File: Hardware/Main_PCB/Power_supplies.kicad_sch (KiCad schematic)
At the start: 21 parts, among them U2 TPS62170DSG, U3 TPS61175PWPR, U7 BD50FD0WFP2-E2

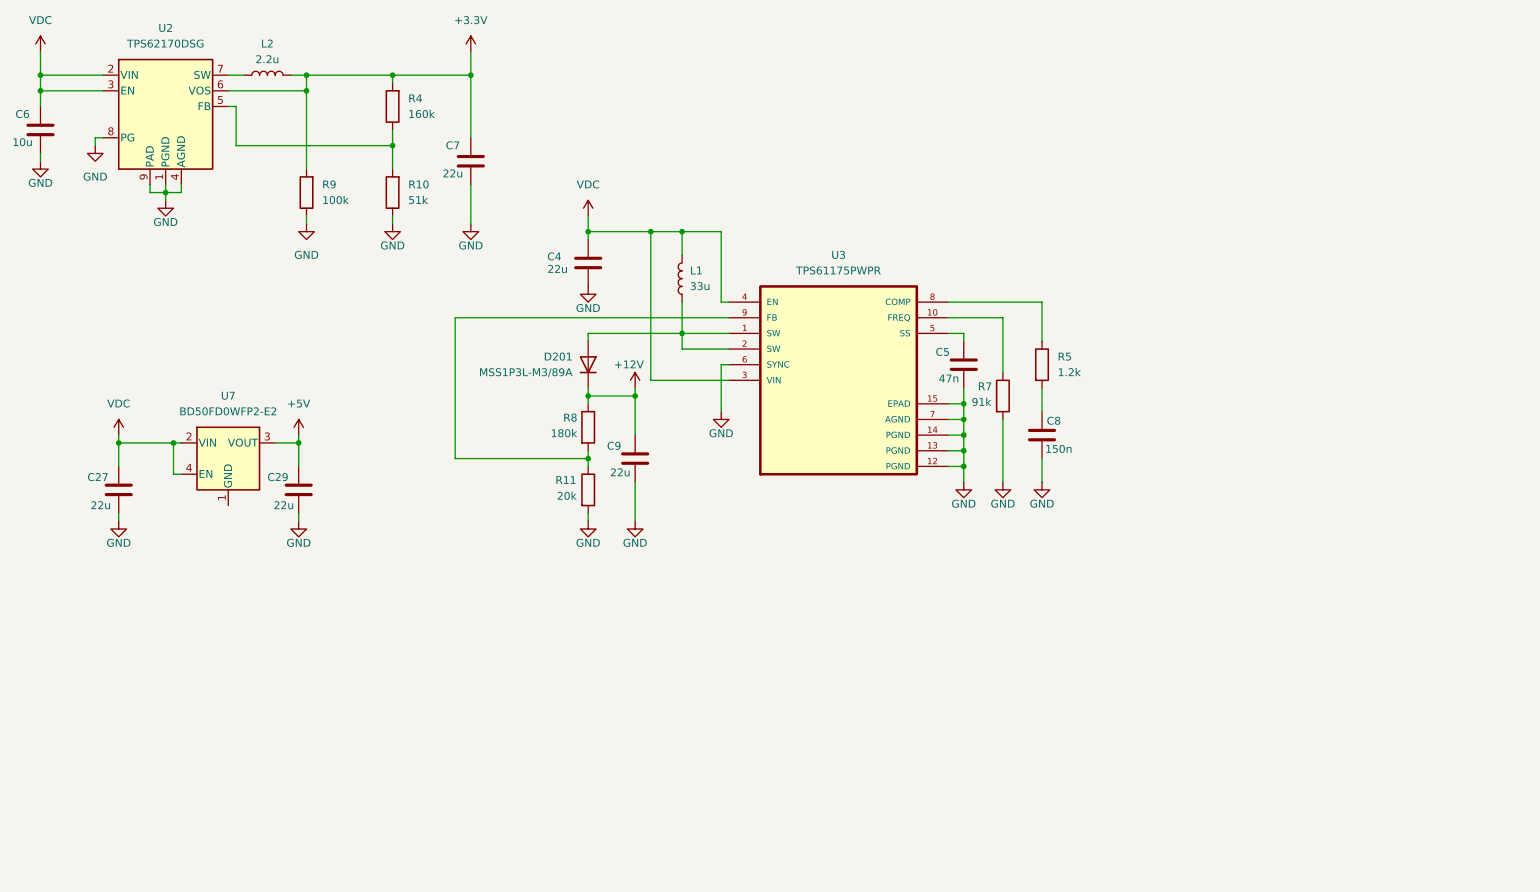
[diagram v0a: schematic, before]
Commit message: A finished version of the Main PCB schematic
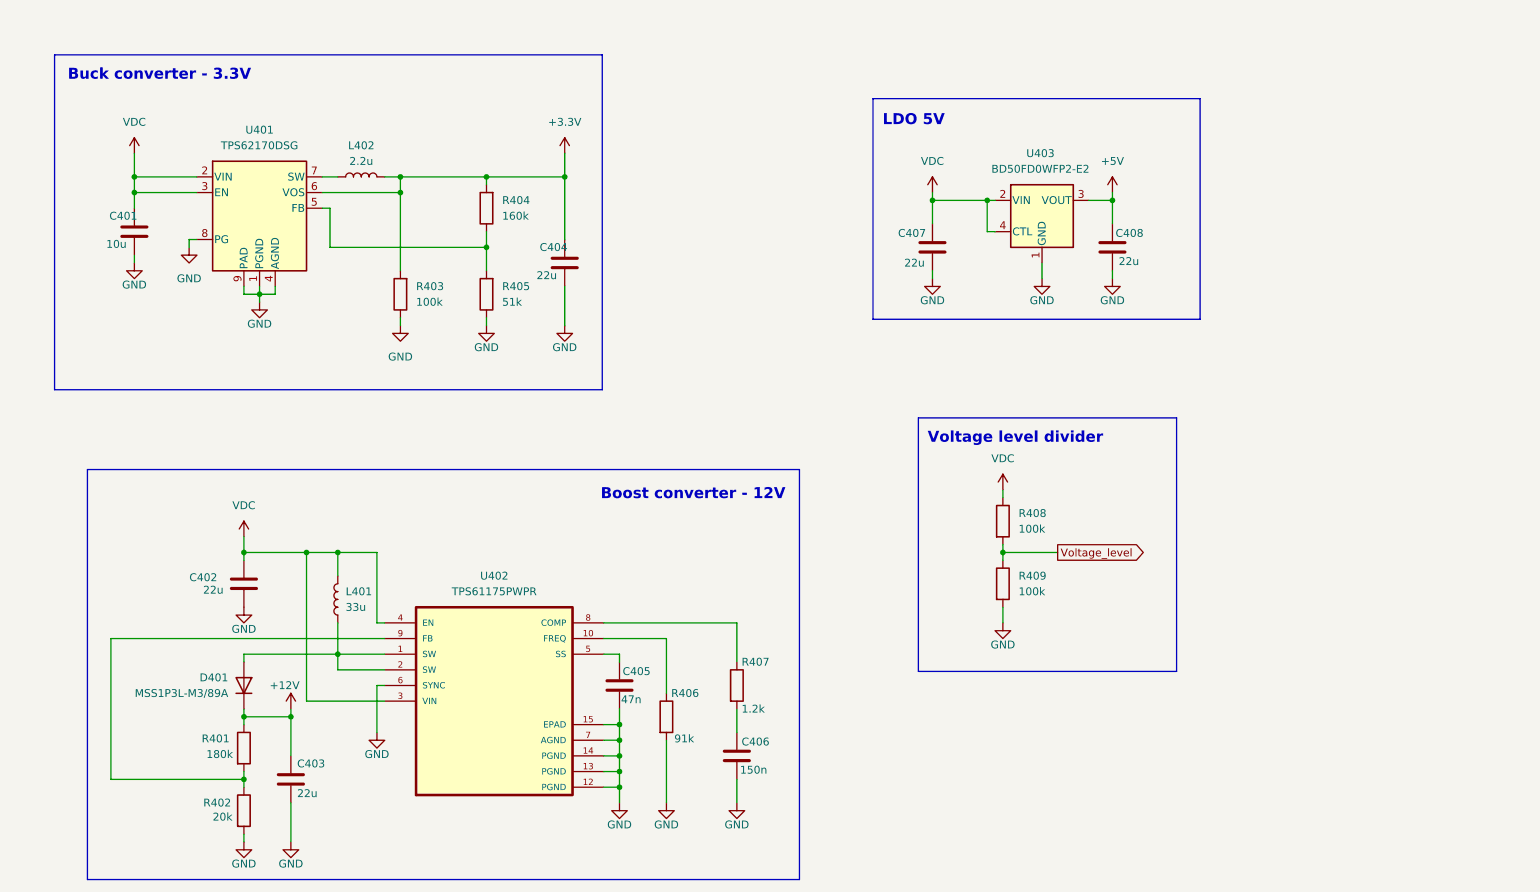
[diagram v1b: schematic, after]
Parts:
- added R408, R409: 100k, Resistor_SMD:R_0603_1608Metric_Pad0.98x0.95mm_HandSolder, symbol Device:R
- renumbered C6 to C401, C4 to C402, C9 to C403, C7 to C404, C5 to C405, C8 to C406, C27 to C407, C29 to C408, D201 to D401, L1 to L401, L2 to L402, R8 to R401, R11 to R402, R9 to R403, R4 to R404, R10 to R405, R7 to R406, R5 to R407, U2 to U401, U3 to U402, U7 to U403
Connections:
- net GND: now also U403.1 (GND), R409.2
- net VDC: now also R408.1
- new net Voltage_level: R408.2, R409.1
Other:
- note added: "Boost converter - 12V"
- note added: "Buck converter - 3.3V"
- note added: "LDO 5V"
- note added: "Voltage level divider"
- moved on the sheet: C401, C402, C403, C404, C405, C406, C407, C408, D401, L401, L402, R401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

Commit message: Added footprints to all components
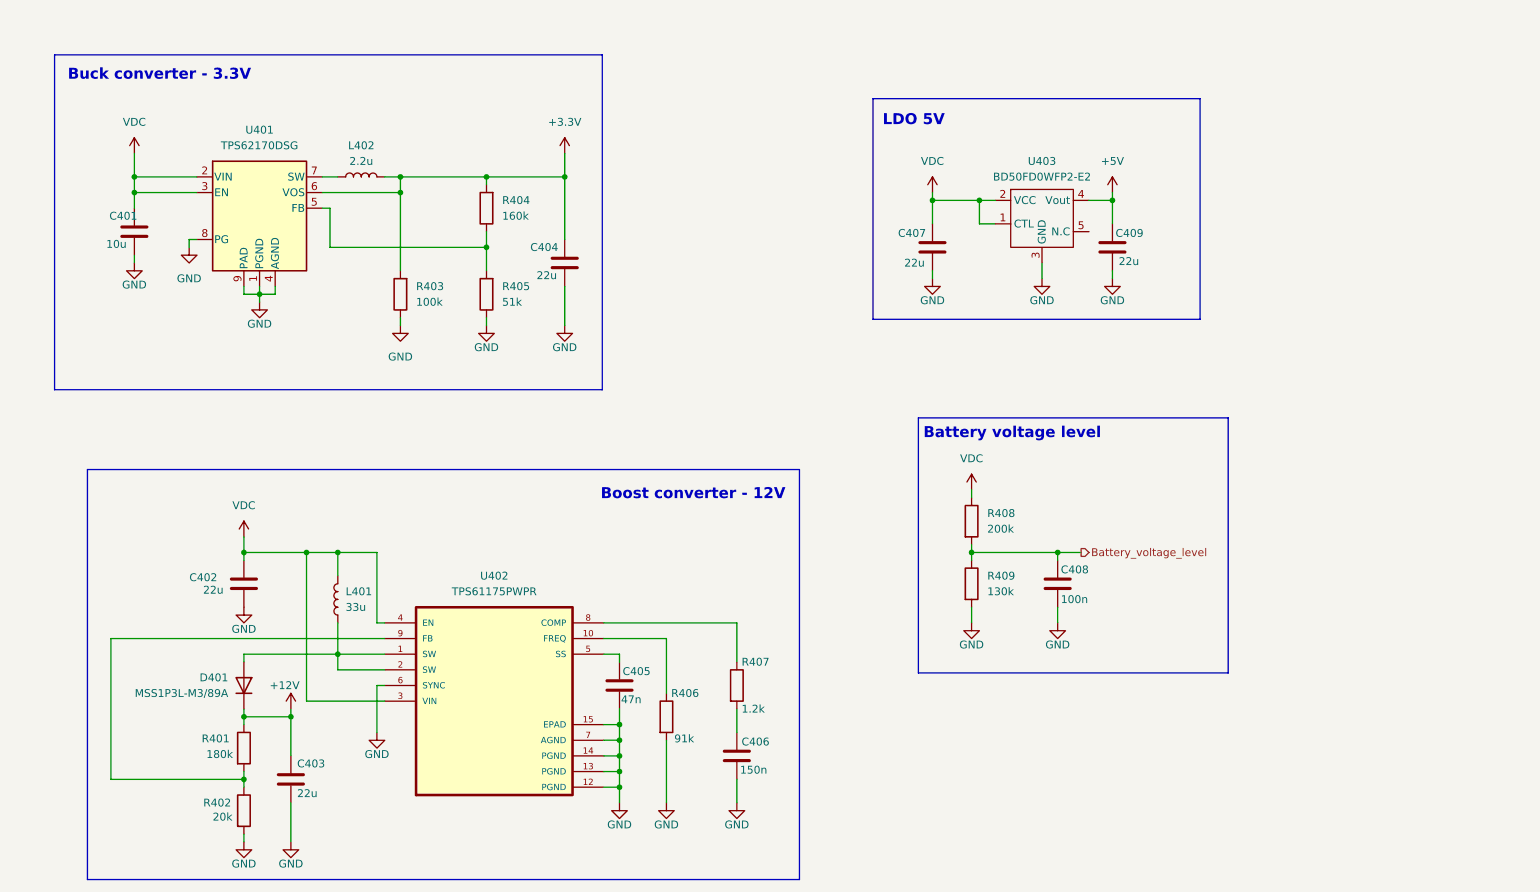
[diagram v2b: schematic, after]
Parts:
- removed U403: BD50FD0WFP2-E2, Package_TO_SOT_SMD:SC-82AB, symbol Regulator_Linear:NCP662SQ50
- added C408: 100n, Capacitor_SMD:C_0603_1608Metric_Pad1.08x0.95mm_HandSolder, symbol Device:C
- added U403: BD50FD0WFP2-E2, Package_TO_SOT_SMD:TO-263-5_TabPin3, symbol MainPCB_Sym_lib:BD50FD0WFP2-E2
- C407: footprint (none) -> Capacitor_SMD:C_0805_2012Metric_Pad1.18x1.45mm_HandSolder
- C409: renamed from C408; footprint (none) -> Capacitor_SMD:C_0805_2012Metric_Pad1.18x1.45mm_HandSolder
- R408: value 100k -> 200k
- R409: value 100k -> 130k
- U402: footprint TPS61175PWPR:IC_TPS27S100BPWPR -> MainPCB:IC_TPS27S100BPWPR
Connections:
- net +5V: now also U403.4 (Vout)
- net GND: now also C408.2, U403.3 (GND)
- net VDC: now also U403.1 (CTL), U403.2 (VCC)
- net Voltage_level renamed Battery_voltage_level
- net Battery_voltage_level: now also C408.1
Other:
- note added: "Battery voltage level"
- note removed: "Voltage level divider"
- moved on the sheet: R408, R409

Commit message: Finished the schematic of the MainPCB
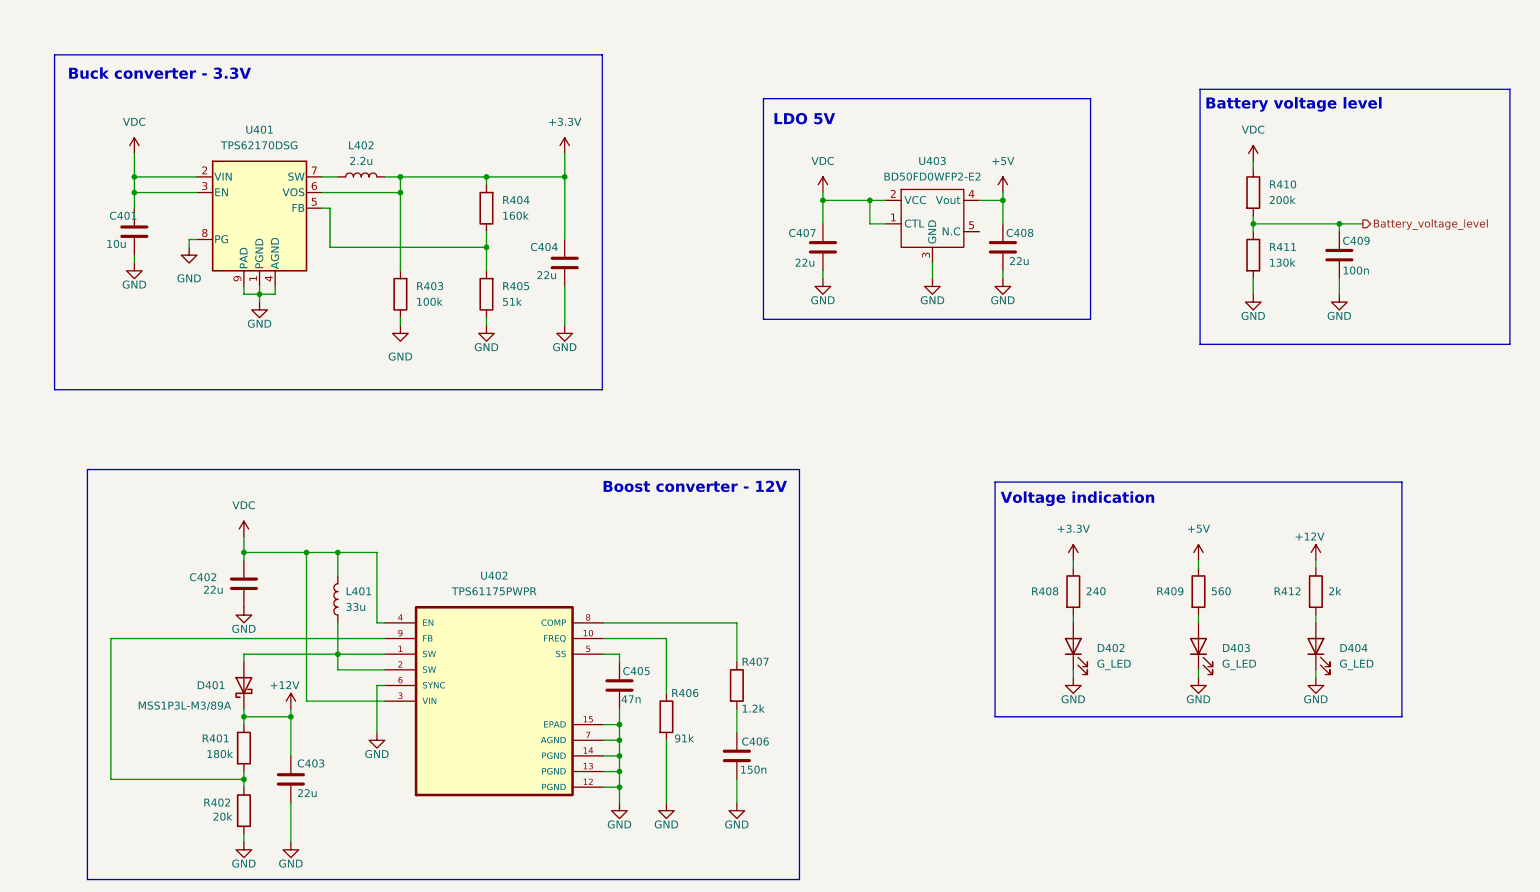
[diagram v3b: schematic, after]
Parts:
- removed D401: MSS1P3L-M3/89A, Diode_SMD:Vishay_SMPA, symbol Diode:S2JTR
- added D401: MSS1P3L-M3/89A, Diode_SMD:Vishay_SMPA, symbol Device:D_Schottky
- added D402, D403, D404: G_LED, Diode_SMD:D_0603_1608Metric_Pad1.05x0.95mm_HandSolder, symbol Device:LED
- added R408: 240, Resistor_SMD:R_0603_1608Metric_Pad0.98x0.95mm_HandSolder, symbol Device:R
- added R409: 560, Resistor_SMD:R_0603_1608Metric_Pad0.98x0.95mm_HandSolder, symbol Device:R
- added R412: 2k, Resistor_SMD:R_0603_1608Metric_Pad0.98x0.95mm_HandSolder, symbol Device:R
- renumbered C409 to C408, C408 to C409, R408 to R410, R409 to R411
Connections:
- net +12V: now also D401.1 (K), R412.1
- net +3.3V: now also R408.1
- net +5V: now also R409.1
- net GND: now also D402.1 (K), D403.1 (K), D404.1 (K)
- net at L401.1, U402.1 (SW), U402.2 (SW): now also D401.2 (A)
- new net: D404.2 (A), R412.2
- new net: D402.2 (A), R408.2
- new net: D403.2 (A), R409.2
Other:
- note added: "Voltage indication"
- moved on the sheet: C407, C408, C409, R410, R411, U403

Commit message: Placement almost complete on MainPCB
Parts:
- L401: footprint MainPCB:IND_SRR6038-100Y -> MainPCB:L_33uH
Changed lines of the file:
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@@
 			)
 		)
-		(property "Footprint" "MainPCB:IND_SRR6038-100Y"
+		(property "Footprint" "MainPCB:L_33uH"
 			(at 71.12 110.49 0)
 			(effects
@@
 			)
 		)
-		(property "Datasheet" "https://docs.rs-online.com/b98a/A700000007859832.pdf"
+		(property "Datasheet" "https://docs.rs-online.com/983b/A700000006423184.pdf"
 			(at 71.12 110.49 0)
 			(effects
@@
 			)
 		)
-		(property "Description" "Inductor"
+		(property "Description" "https://dk.rs-online.com/web/p/smd-spoler/8987889"
 			(at 71.12 110.49 0)
 			(effects

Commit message: V1.1 of the MainPCB
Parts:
- L401: footprint MainPCB:L_33uH -> MainPCB:VLCF4018
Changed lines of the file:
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@@
 			)
 		)
-		(property "Footprint" "MainPCB:L_33uH"
+		(property "Footprint" "MainPCB:VLCF4018"
 			(at 71.12 110.49 0)
 			(effects
@@
 			)
 		)
-		(property "Datasheet" "https://docs.rs-online.com/983b/A700000006423184.pdf"
+		(property "Datasheet" "https://docs.rs-online.com/18c7/0900766b81538d88.pdf"
 			(at 71.12 110.49 0)
 			(effects
@@
 		(dnp no)
 		(property "Reference" "C401"
-			(at 34.036 48.26 0)
-			(effects
-				(font
+			(at 32.766 48.26 0)
+			(effects
+				(font

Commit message: Finished MainPCB v3
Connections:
- net VDC renamed +VPROT
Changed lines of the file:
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@@
 		(on_board yes)
 		(dnp no)
-		(fields_autoplaced yes)
 		(property "Reference" "#PWR0418"
 			(at 149.86 48.26 0)
@@
 			)
 		)
-		(property "Value" "VDC"
-			(at 149.86 39.37 0)
-			(effects
-				(font
-					(size 1.27 1.27)
-				)
+		(property "Value" "+VPROT"
+			(at 145.796 40.64 0)
+			(effects
+				(font
+					(size 1.27 1.27)
+				)
+				(justify left)
 			)
 		)
@@
 		(on_board yes)
 		(dnp no)
-		(fields_autoplaced yes)
 		(property "Reference" "#PWR0401"
 			(at 38.1 41.91 0)
@@
 			)
 		)
-		(property "Value" "VDC"
-			(at 38.1 33.02 0)
-			(effects
-				(font
-					(size 1.27 1.27)
-				)
+		(property "Value" "+VPROT"
+			(at 34.036 34.29 0)
+			(effects
+				(font
+					(size 1.27 1.27)
+				)
+				(justify left)
 			)
 		)
@@
 		(on_board yes)
 		(dnp no)
-		(fields_autoplaced yes)
 		(property "Reference" "#PWR0427"
 			(at 219.71 43.18 0)
@@
 			)
 		)
-		(property "Value" "VDC"
-			(at 219.71 34.29 0)
-			(effects
-				(font
-					(size 1.27 1.27)
-				)
+		(property "Value" "+VPROT"
+			(at 215.9 35.56 0)
+			(effects
+				(font
+					(size 1.27 1.27)
+				)
+				(justify left)
 			)
 		)
@@
 		(on_board yes)
 		(dnp no)
-		(fields_autoplaced yes)
 		(property "Reference" "#PWR0404"
 			(at 55.88 104.14 0)
@@
 			)
 		)
-		(property "Value" "VDC"
-			(at 55.88 95.25 0)
-			(effects
-				(font
-					(size 1.27 1.27)
-				)
-			)
-		)
+		(property "Value" "+VPROT"
+			(at 52.07 96.52 0)
+			(effects
+				(font
+					(size 1.27 1.27)
+				)
+				(justify left)
+			)
+		)

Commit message: Beautifying the Master Controller
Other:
- company: (none) -> Made by Liubomir Stanev
- title: (none) -> Master controller
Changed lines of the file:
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@@
 	(generator_version "9.0")
 	(paper "A4")
+	(title_block
+		(title "Master controller")
+		(date "22/12/2025")
+		(company "Made by Liubomir Stanev")
+		(comment 1 "Page 4: Power supply unit")
+	)
 	(rectangle
 		(start 25.146 22.098)
